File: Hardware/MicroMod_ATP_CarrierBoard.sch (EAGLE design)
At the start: 57 parts, among them J19 QWIIC_RIGHT_ANGLE, J2 JTAG, J20 QWIIC_RIGHT_ANGLE, J21 1X04_SMD_STRAIGHT_COMBO, J23 1X04_SMD_STRAIGHT_COMBO, J4 USB_A_SMT_FEMALE, J6 MICROMOD-2222-C, J8 1X04_SMD_STRAIGHT_COMBO, U5 AP7361C-33

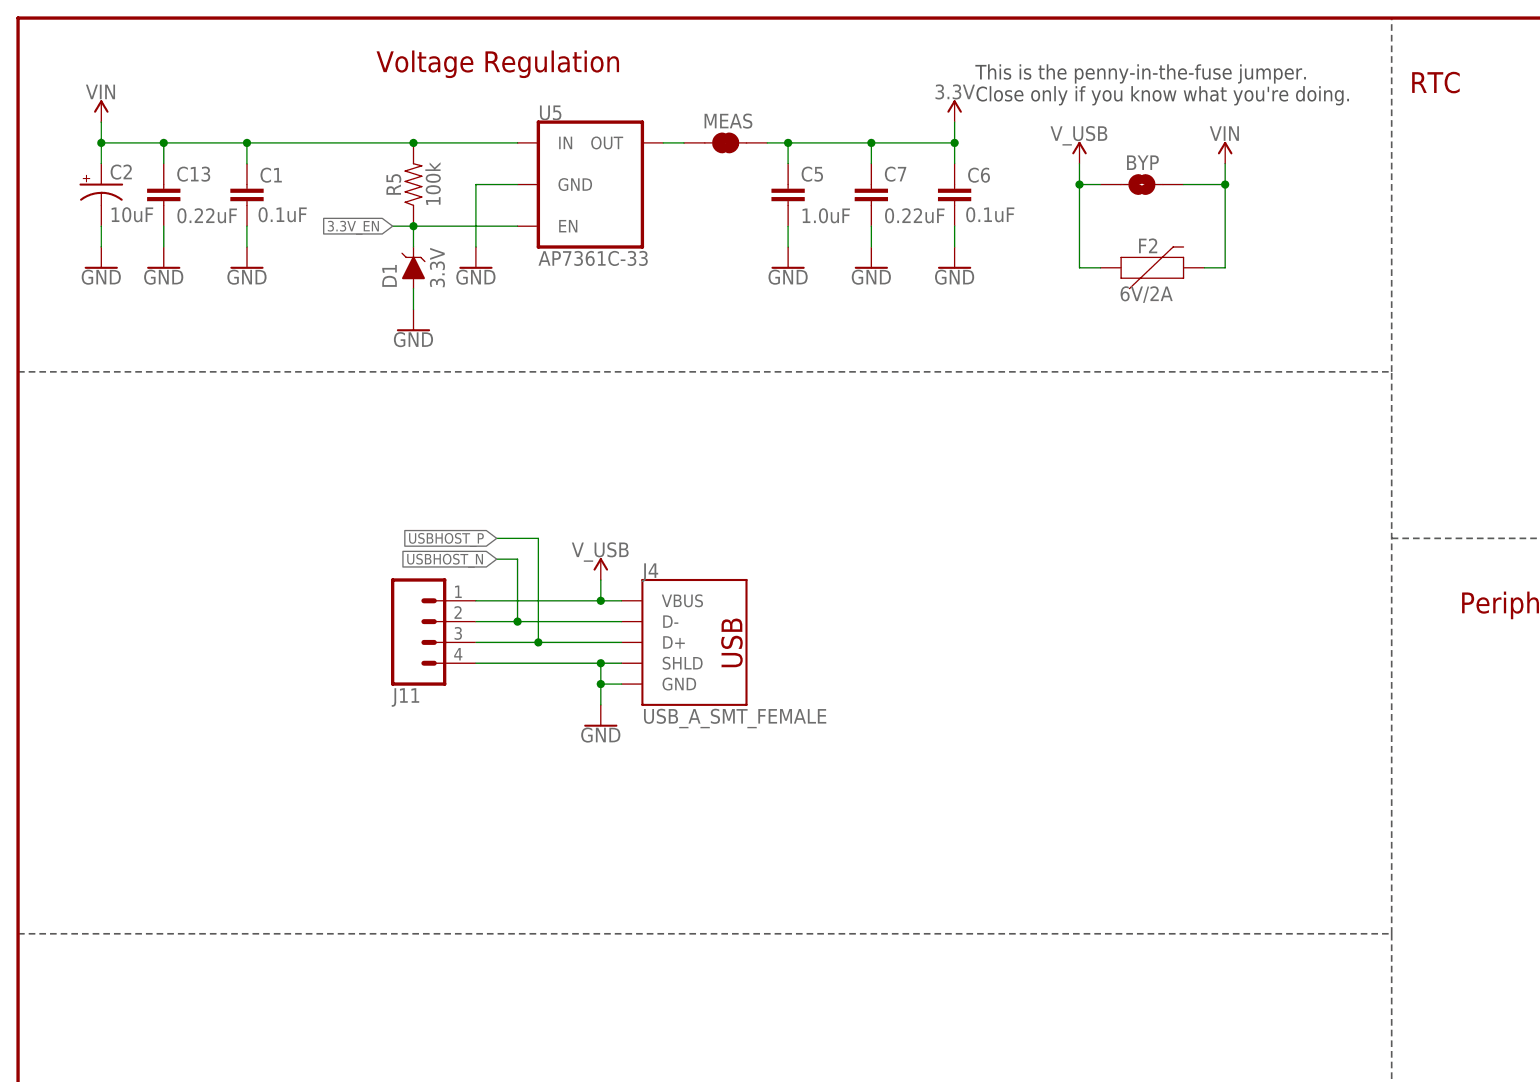
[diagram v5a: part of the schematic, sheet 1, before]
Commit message: Routes the Analog and RX2 traces
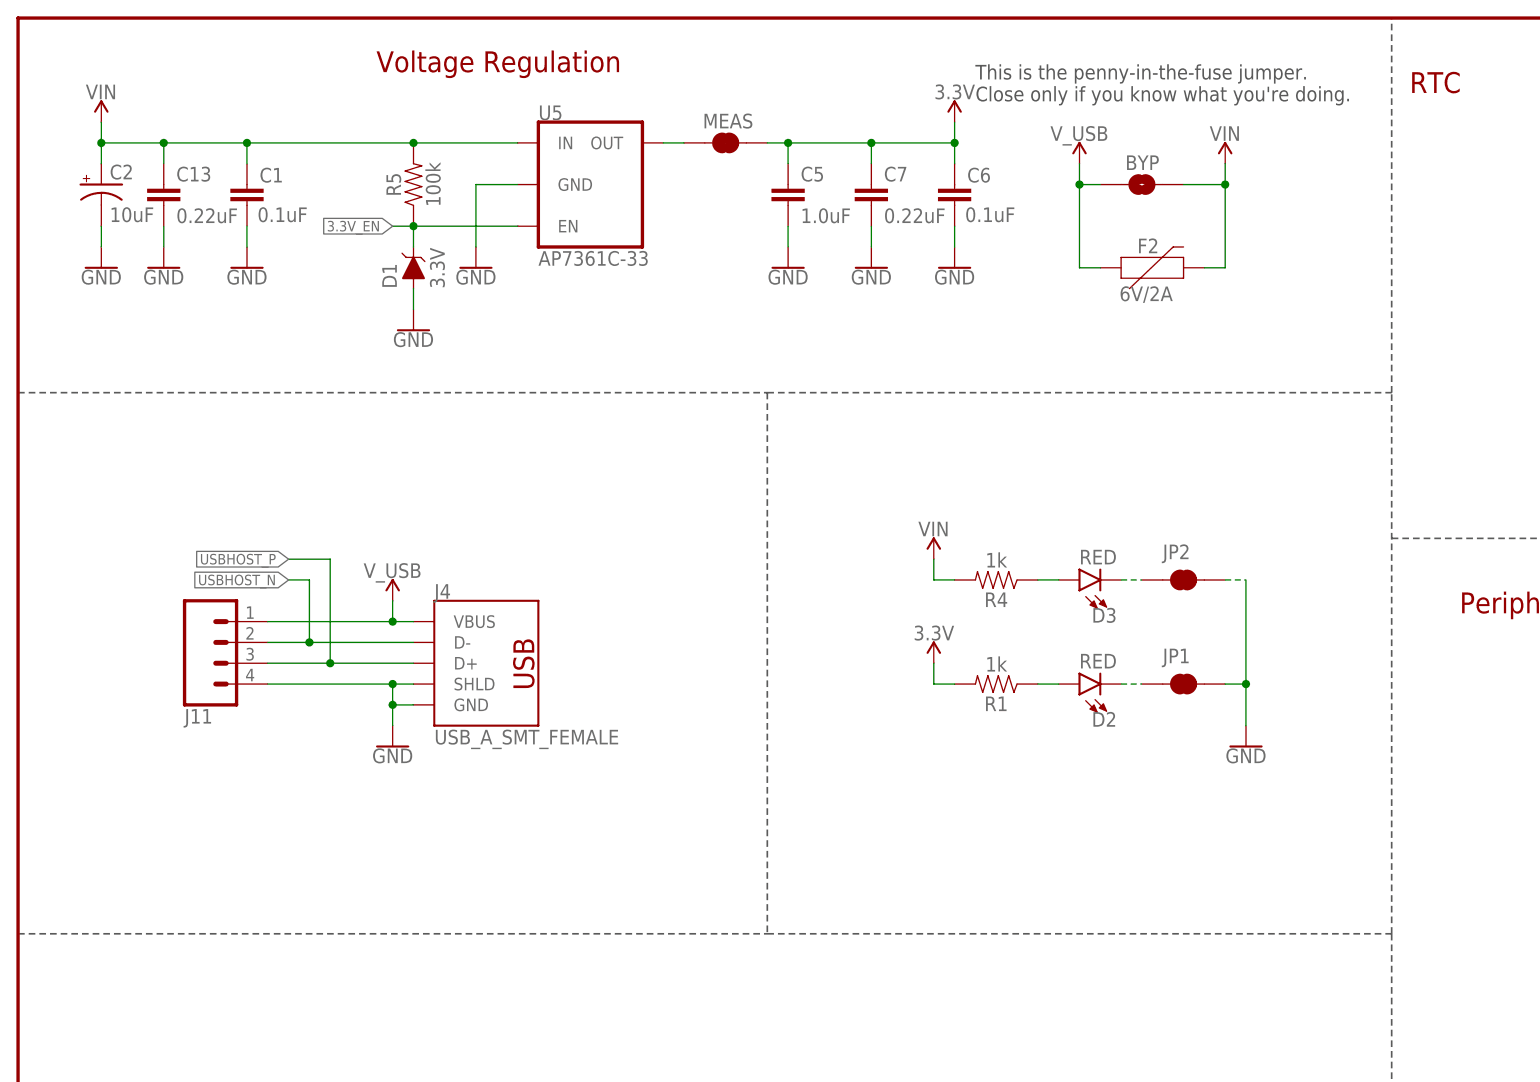
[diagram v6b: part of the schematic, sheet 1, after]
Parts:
- added D2, D3: RED, SparkFun-LED:LED-RED0603
- added JP1, JP2: JUMPER-SMT_2_NC_TRACE_SILK, SparkFun-Jumpers:JUMPER-SMT_2_NC_TRACE_SILK
- added R1, R4: 1k, SparkFun-Resistors:1KOHM-0603-1/10W-1%
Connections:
- new net N$1: D2.A, R1.1
- new net N$2: D3.A, R4.1
- new net N$3: D2.C, JP1.1
- new net N$4: D3.C, JP2.1
- net 3.3V: now also R1.2
- net GND: now also JP1.2, JP2.2
- net VIN: now also R4.2
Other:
- moved on the sheet: J11, J4

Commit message: Routes Serial, I2C, and CAN lines
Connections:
- net CAN_RXI: now also J25.1, J5.9; no longer J25.2, J5.10
- net CAN_TXO: now also J25.2, J5.10; no longer J25.1, J5.9
- net CTS1: now also J24.6, J5.6; no longer J24.5, J5.5
- net RTS1: now also J24.5, J5.5; no longer J24.6, J5.6
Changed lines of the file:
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@@
-</segment>
-<segment>
-<wire x1="254" y1="101.6" x2="256.54" y2="101.6" width="0.1524" layer="91" style="longdash"/>
-<pinref part="J25" gate="G$1" pin="1"/>
-<wire x1="279.4" y1="104.14" x2="276.86" y2="104.14" width="0.1524" layer="91" style="longdash"/>
-<pinref part="J5" gate="G$1" pin="9"/>
-<wire x1="256.54" y1="101.6" x2="256.54" y2="104.14" width="0.1524" layer="91"/>
-<wire x1="256.54" y1="104.14" x2="261.62" y2="104.14" width="0.1524" layer="91"/>
-<wire x1="261.62" y1="104.14" x2="276.86" y2="104.14" width="0.1524" layer="91"/>
-<wire x1="261.62" y1="104.14" x2="261.62" y2="63.5" width="0.1524" layer="91"/>
-<wire x1="261.62" y1="63.5" x2="279.4" y2="63.5" width="0.1524" layer="91"/>
-<junction x="261.62" y="104.14"/>
-<label x="279.4" y="63.5" size="1.27" layer="95" xref="yes"/>
-</segment>
-</net>
-<net name="CAN_RXI" class="0">
-<segment>
-<wire x1="33.02" y1="93.98" x2="30.48" y2="93.98" width="0.1524" layer="91"/>
-<label x="30.48" y="93.98" size="1.27" layer="95" rot="R180" xref="yes"/>
-<pinref part="J6" gate="J1" pin="CAN-RX"/>
 </segment>
 <segment>
@@
 </segment>
 </net>
+<net name="CAN_RXI" class="0">
+<segment>
+<wire x1="33.02" y1="93.98" x2="30.48" y2="93.98" width="0.1524" layer="91"/>
+<label x="30.48" y="93.98" size="1.27" layer="95" rot="R180" xref="yes"/>
+<pinref part="J6" gate="J1" pin="CAN-RX"/>
+</segment>
+<segment>
+<wire x1="254" y1="101.6" x2="256.54" y2="101.6" width="0.1524" layer="91" style="longdash"/>
+<pinref part="J25" gate="G$1" pin="1"/>
+<wire x1="279.4" y1="104.14" x2="276.86" y2="104.14" width="0.1524" layer="91" style="longdash"/>
+<pinref part="J5" gate="G$1" pin="9"/>
+<wire x1="256.54" y1="101.6" x2="256.54" y2="104.14" width="0.1524" layer="91"/>
+<wire x1="256.54" y1="104.14" x2="261.62" y2="104.14" width="0.1524" layer="91"/>
+<wire x1="261.62" y1="104.14" x2="276.86" y2="104.14" width="0.1524" layer="91"/>
+<wire x1="261.62" y1="104.14" x2="261.62" y2="63.5" width="0.1524" layer="91"/>
+<wire x1="261.62" y1="63.5" x2="279.4" y2="63.5" width="0.1524" layer="91"/>
+<junction x="261.62" y="104.14"/>
+<label x="279.4" y="63.5" size="1.27" layer="95" xref="yes"/>
+</segment>
+</net>
 <net name="MOSI1" class="0">
 <segment>
@@
 <wire x1="78.74" y1="78.74" x2="81.28" y2="78.74" width="0.1524" layer="91"/>
 <label x="81.28" y="78.74" size="1.27" layer="95" xref="yes"/>
+</segment>
+<segment>
+<wire x1="254" y1="114.3" x2="251.46" y2="114.3" width="0.1524" layer="91"/>
+<pinref part="J24" gate="G$1" pin="5"/>
+<pinref part="J5" gate="G$1" pin="5"/>
+<wire x1="254" y1="114.3" x2="266.7" y2="114.3" width="0.1524" layer="91"/>
+<wire x1="266.7" y1="114.3" x2="279.4" y2="114.3" width="0.1524" layer="91"/>
+<wire x1="266.7" y1="114.3" x2="266.7" y2="139.7" width="0.1524" layer="91"/>
+<wire x1="266.7" y1="139.7" x2="279.4" y2="139.7" width="0.1524" layer="91"/>
+<junction x="266.7" y="114.3"/>
+<label x="279.4" y="139.7" size="1.27" layer="95" xref="yes"/>
+</segment>
+</net>
+<net name="CTS1" class="0">
+<segment>
+<pinref part="J6" gate="J1" pin="CTS1"/>
+<wire x1="78.74" y1="76.2" x2="81.28" y2="76.2" width="0.1524" layer="91"/>
+<label x="81.28" y="76.2" size="1.27" layer="95" xref="yes"/>
 </segment>
 <segment>
@@
 </segment>
 </net>
-<net name="CTS1" class="0">
-<segment>
-<pinref part="J6" gate="J1" pin="CTS1"/>
-<wire x1="78.74" y1="76.2" x2="81.28" y2="76.2" width="0.1524" layer="91"/>
-<label x="81.28" y="76.2" size="1.27" layer="95" xref="yes"/>
-</segment>
-<segment>
-<wire x1="254" y1="114.3" x2="251.46" y2="114.3" width="0.1524" layer="91"/>
-<pinref part="J24" gate="G$1" pin="5"/>
-<pinref part="J5" gate="G$1" pin="5"/>
-<wire x1="254" y1="114.3" x2="266.7" y2="114.3" width="0.1524" layer="91"/>
-<wire x1="266.7" y1="114.3" x2="279.4" y2="114.3" width="0.1524" layer="91"/>
-<wire x1="266.7" y1="114.3" x2="266.7" y2="139.7" width="0.1524" layer="91"/>
-<wire x1="266.7" y1="139.7" x2="279.4" y2="139.7" width="0.1524" layer="91"/>
-<junction x="266.7" y="114.3"/>
-<label x="279.4" y="139.7" size="1.27" layer="95" xref="yes"/>
-</segment>
-</net>

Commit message: Reorders the "G#" lines and moves traces so that they hit at 90 degrees
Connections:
- net SD_!CS! renamed !CS!
- net G0: now also J14.7, J15.2; no longer J17.1, J18.8
- net G1: now also J14.8, J15.1; no longer J17.2, J18.7
- net G11: now also J17.8, J18.1; no longer J14.8, J15.1
- net G2: now also J17.1, J18.8; no longer J17.3, J18.6
- net G3: now also J17.2, J18.7; no longer J17.4, J18.5
- net G4: now also J17.3, J18.6; no longer J17.5, J18.4
- net G5: now also J17.4, J18.5; no longer J17.6, J18.3
- net G6: now also J17.5, J18.4; no longer J17.7, J18.2
- net G7: now also J17.6, J18.3; no longer J17.8, J18.1
- net G8: now also J17.7, J18.2; no longer J14.7, J15.2
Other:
- moved on the sheet: BT1, D6, D7, H5, R8, S1, S2
